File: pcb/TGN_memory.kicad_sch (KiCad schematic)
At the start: 24 parts, among them J10 Conn_01x08_Pin, J11 Conn_01x03_Pin, J12 Conn_01x03_Pin, U10 SST39SF040

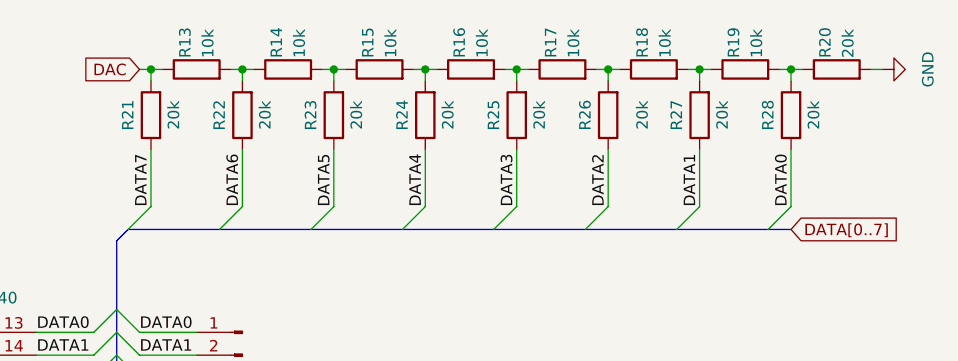
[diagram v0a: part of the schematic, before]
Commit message: Adapt ladder resistor values
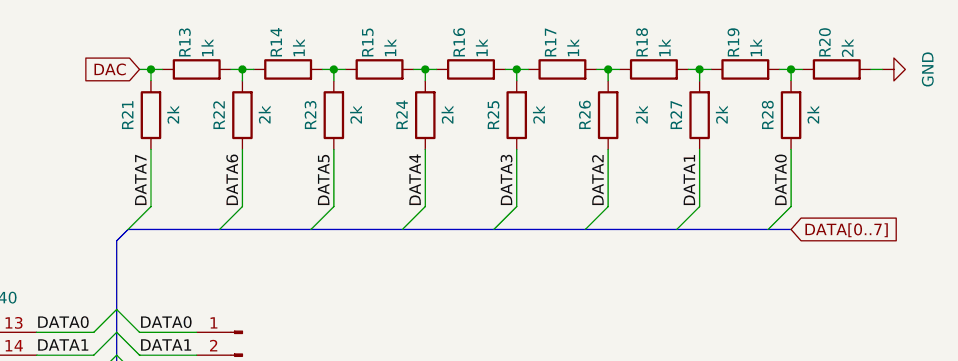
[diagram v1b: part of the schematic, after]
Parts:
- R13, R14, R15, R16, R17, R18, R19: value 10k -> 1k; VendorId 102812 -> 102800
- R20, R21, R22, R23, R24, R25, R26, R27, R28: value 20k -> 2k; VendorId 13-MFR-25FRF52-20KCT-ND -> 13-MFR-25FRF52-2KCT-ND
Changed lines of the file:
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@@
       (effects (font (size 1.27 1.27)) (justify left))
     )
-    (property "Value" "10k" (at 162.56 54.61 0)
+    (property "Value" "1k" (at 162.56 54.61 0)
       (effects (font (size 1.27 1.27)) (justify left))
     )
@@
       (effects (font (size 1.27 1.27)) hide)
     )
-    (property "VendorId" "102812" (at 161.29 55.88 0)
+    (property "VendorId" "102800" (at 161.29 55.88 0)
       (effects (font (size 1.27 1.27)) hide)
     )
@@
       (effects (font (size 1.27 1.27)) (justify left))
     )
-    (property "Value" "20k" (at 233.68 54.61 0)
+    (property "Value" "2k" (at 233.68 54.61 0)
       (effects (font (size 1.27 1.27)) (justify left))
     )
@@
       (effects (font (size 1.27 1.27)) hide)
     )
-    (property "VendorId" "13-MFR-25FRF52-20KCT-ND" (at 232.41 55.88 0)
+    (property "VendorId" "13-MFR-25FRF52-2KCT-ND" (at 232.41 55.88 0)
       (effects (font (size 1.27 1.27)) hide)
     )
@@
       (effects (font (size 1.27 1.27)))
     )
-    (property "Value" "20k" (at 229.87 60.96 90)
+    (property "Value" "2k" (at 229.87 60.96 90)
       (effects (font (size 1.27 1.27)))
     )
@@
       (effects (font (size 1.27 1.27)) hide)
     )
-    (property "VendorId" "13-MFR-25FRF52-20KCT-ND" (at 227.33 60.96 0)
+    (property "VendorId" "13-MFR-25FRF52-2KCT-ND" (at 227.33 60.96 0)
       (effects (font (size 1.27 1.27)) hide)
     )
@@
       (effects (font (size 1.27 1.27)) (justify left))
     )
-    (property "Value" "10k" (at 182.88 54.61 0)
+    (property "Value" "1k" (at 182.88 54.61 0)
       (effects (font (size 1.27 1.27)) (justify left))
     )
@@
       (effects (font (size 1.27 1.27)) hide)
     )
-    (property "VendorId" "102812" (at 181.61 55.88 0)
+    (property "VendorId" "102800" (at 181.61 55.88 0)
       (effects (font (size 1.27 1.27)) hide)
     )
@@
       (effects (font (size 1.27 1.27)))
     )
-    (property "Value" "20k" (at 210.82 60.96 90)
+    (property "Value" "2k" (at 210.82 60.96 90)
       (effects (font (size 1.27 1.27)))
     )
@@
       (effects (font (size 1.27 1.27)) hide)
     )
-    (property "VendorId" "13-MFR-25FRF52-20KCT-ND" (at 207.01 60.96 0)
+    (property "VendorId" "13-MFR-25FRF52-2KCT-ND" (at 207.01 60.96 0)
       (effects (font (size 1.27 1.27)) hide)
     )
@@
       (effects (font (size 1.27 1.27)))
     )
-    (property "Value" "20k" (at 168.91 60.96 90)
+    (property "Value" "2k" (at 168.91 60.96 90)
       (effects (font (size 1.27 1.27)))
     )
@@
       (effects (font (size 1.27 1.27)) hide)
     )
-    (property "VendorId" "13-MFR-25FRF52-20KCT-ND" (at 166.37 60.96 0)
+    (property "VendorId" "13-MFR-25FRF52-2KCT-ND" (at 166.37 60.96 0)
       (effects (font (size 1.27 1.27)) hide)
     )
@@
       (effects (font (size 1.27 1.27)) (justify left))
     )
-    (property "Value" "10k" (at 172.72 54.61 0)
+    (property "Value" "1k" (at 172.72 54.61 0)
       (effects (font (size 1.27 1.27)) (justify left))
     )
@@
       (effects (font (size 1.27 1.27)) hide)
     )
-    (property "VendorId" "102812" (at 171.45 55.88 0)
+    (property "VendorId" "102800" (at 171.45 55.88 0)
       (effects (font (size 1.27 1.27)) hide)
     )
@@
       (effects (font (size 1.27 1.27)))
     )
-    (property "Value" "20k" (at 219.71 60.96 90)
+    (property "Value" "2k" (at 219.71 60.96 90)
       (effects (font (size 1.27 1.27)))
     )
@@
       (effects (font (size 1.27 1.27)) hide)
     )
-    (property "VendorId" "13-MFR-25FRF52-20KCT-ND" (at 217.17 60.96 0)
+    (property "VendorId" "13-MFR-25FRF52-2KCT-ND" (at 217.17 60.96 0)
       (effects (font (size 1.27 1.27)) hide)
     )
@@
       (effects (font (size 1.27 1.27)) (justify left))
     )
-    (property "Value" "10k" (at 213.36 54.61 0)
+    (property "Value" "1k" (at 213.36 54.61 0)
       (effects (font (size 1.27 1.27)) (justify left))
     )
@@
       (effects (font (size 1.27 1.27)) hide)
     )
-    (property "VendorId" "102812" (at 212.09 55.88 0)
+    (property "VendorId" "102800" (at 212.09 55.88 0)
       (effects (font (size 1.27 1.27)) hide)
     )
@@
       (effects (font (size 1.27 1.27)) (justify left))
     )
-    (property "Value" "10k" (at 203.2 54.61 0)
+    (property "Value" "1k" (at 203.2 54.61 0)
       (effects (font (size 1.27 1.27)) (justify left))
     )
@@
       (effects (font (size 1.27 1.27)) hide)
     )
-    (property "VendorId" "102812" (at 201.93 55.88 0)
+    (property "VendorId" "102800" (at 201.93 55.88 0)
       (effects (font (size 1.27 1.27)) hide)
     )
@@
       (effects (font (size 1.27 1.27)) (justify left))
     )
-    (property "Value" "10k" (at 223.52 54.61 0)
+    (property "Value" "1k" (at 223.52 54.61 0)
       (effects (font (size 1.27 1.27)) (justify left))
     )
@@
       (effects (font (size 1.27 1.27)) hide)
     )
-    (property "VendorId" "102812" (at 222.25 55.88 0)
+    (property "VendorId" "102800" (at 222.25 55.88 0)
       (effects (font (size 1.27 1.27)) hide)
     )
@@
       (effects (font (size 1.27 1.27)))
     )
-    (property "Value" "20k" (at 158.75 60.96 90)
+    (property "Value" "2k" (at 158.75 60.96 90)
       (effects (font (size 1.27 1.27)))
     )
@@
       (effects (font (size 1.27 1.27)) hide)
     )
-    (property "VendorId" "13-MFR-25FRF52-20KCT-ND" (at 156.21 60.96 0)
+    (property "VendorId" "13-MFR-25FRF52-2KCT-ND" (at 156.21 60.96 0)
       (effects (font (size 1.27 1.27)) hide)
     )
@@
       (effects (font (size 1.27 1.27)))
     )
-    (property "Value" "20k" (at 199.39 60.96 90)
+    (property "Value" "2k" (at 199.39 60.96 90)
       (effects (font (size 1.27 1.27)))
     )
@@
       (effects (font (size 1.27 1.27)) hide)
     )
-    (property "VendorId" "13-MFR-25FRF52-20KCT-ND" (at 196.85 60.96 0)
+    (property "VendorId" "13-MFR-25FRF52-2KCT-ND" (at 196.85 60.96 0)
       (effects (font (size 1.27 1.27)) hide)
     )
@@
       (effects (font (size 1.27 1.27)))
     )
-    (property "Value" "20k" (at 179.07 60.96 90)
+    (property "Value" "2k" (at 179.07 60.96 90)
       (effects (font (size 1.27 1.27)))
     )
@@
       (effects (font (size 1.27 1.27)) hide)
     )
-    (property "VendorId" "13-MFR-25FRF52-20KCT-ND" (at 176.53 60.96 0)
+    (property "VendorId" "13-MFR-25FRF52-2KCT-ND" (at 176.53 60.96 0)
       (effects (font (size 1.27 1.27)) hide)
     )
@@
       (effects (font (size 1.27 1.27)) (justify left))
     )
-    (property "Value" "10k" (at 193.04 54.61 0)
+    (property "Value" "1k" (at 193.04 54.61 0)
       (effects (font (size 1.27 1.27)) (justify left))
     )
@@
       (effects (font (size 1.27 1.27)) hide)
     )
-    (property "VendorId" "102812" (at 191.77 55.88 0)
+    (property "VendorId" "102800" (at 191.77 55.88 0)
       (effects (font (size 1.27 1.27)) hide)
     )
@@
       (effects (font (size 1.27 1.27)))
     )
-    (property "Value" "20k" (at 189.23 60.96 90)
+    (property "Value" "2k" (at 189.23 60.96 90)
       (effects (font (size 1.27 1.27)))
     )
@@
       (effects (font (size 1.27 1.27)) hide)
     )
-    (property "VendorId" "13-MFR-25FRF52-20KCT-ND" (at 186.69 60.96 0)
-      (effects (font (size 1.27 1.27)) hide)
-    )
+    (property "VendorId" "13-MFR-25FRF52-2KCT-ND" (at 186.69 60.96 0)
+      (effects (font (size 1.27 1.27)) hide)
+    )
